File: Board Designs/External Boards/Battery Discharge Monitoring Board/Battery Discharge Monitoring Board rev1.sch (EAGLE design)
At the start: 75 parts

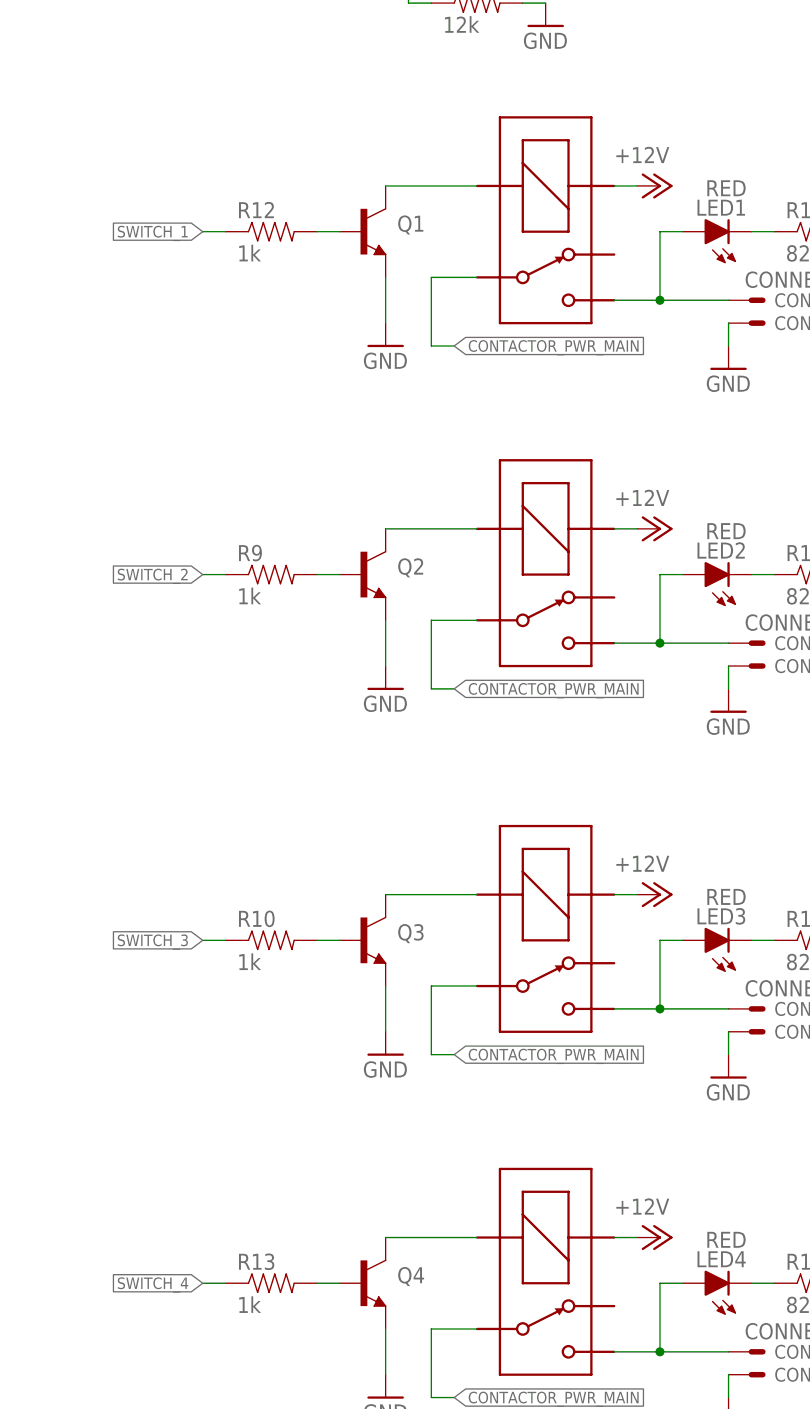
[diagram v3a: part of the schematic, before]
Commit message: Added value for BJTs indicating part number
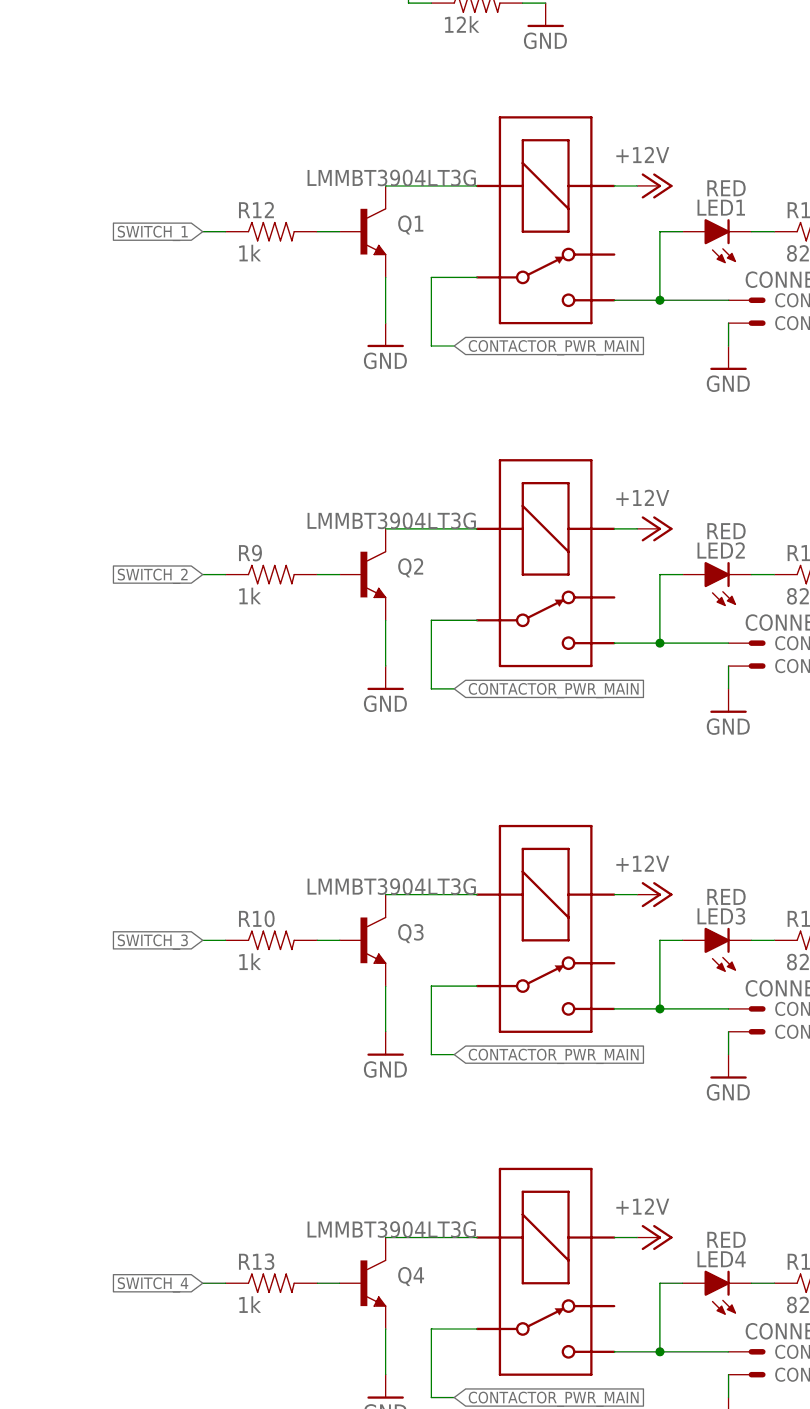
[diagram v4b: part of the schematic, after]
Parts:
- Q1, Q2, Q3, Q4: value (none) -> LMMBT3904LT3G
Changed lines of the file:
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@@
 <part name="P+14" library="supply1" library_urn="urn:adsk.eagle:library:371" deviceset="+5V" device=""/>
 <part name="R11" library="HyTechDevices" deviceset="RESISTOR" device="0805-RES" value="120"/>
-<part name="Q1" library="HyTechDevices" deviceset="BJT_NPN" device="SOT"/>
+<part name="Q1" library="HyTechDevices" deviceset="BJT_NPN" device="SOT" value="LMMBT3904LT3G"/>
 <part name="R12" library="HyTechDevices" deviceset="RESISTOR" device="0805-RES" value="1k"/>
 <part name="GND29" library="supply1" library_urn="urn:adsk.eagle:library:371" deviceset="GND" device=""/>
@@
 <part name="GND30" library="supply1" library_urn="urn:adsk.eagle:library:371" deviceset="GND" device=""/>
 <part name="GND26" library="supply1" library_urn="urn:adsk.eagle:library:371" deviceset="GND" device=""/>
-<part name="Q2" library="HyTechDevices" deviceset="BJT_NPN" device="SOT"/>
+<part name="Q2" library="HyTechDevices" deviceset="BJT_NPN" device="SOT" value="LMMBT3904LT3G"/>
 <part name="R9" library="HyTechDevices" deviceset="RESISTOR" device="0805-RES" value="1k"/>
 <part name="GND31" library="supply1" library_urn="urn:adsk.eagle:library:371" deviceset="GND" device=""/>
@@
 <part name="CONT_2" library="HyTechDevices" deviceset="CONNECTOR-2" device=""/>
 <part name="GND32" library="supply1" library_urn="urn:adsk.eagle:library:371" deviceset="GND" device=""/>
-<part name="Q3" library="HyTechDevices" deviceset="BJT_NPN" device="SOT"/>
+<part name="Q3" library="HyTechDevices" deviceset="BJT_NPN" device="SOT" value="LMMBT3904LT3G"/>
 <part name="R10" library="HyTechDevices" deviceset="RESISTOR" device="0805-RES" value="1k"/>
 <part name="GND33" library="supply1" library_urn="urn:adsk.eagle:library:371" deviceset="GND" device=""/>
@@
 <part name="CONT_3" library="HyTechDevices" deviceset="CONNECTOR-2" device=""/>
 <part name="GND34" library="supply1" library_urn="urn:adsk.eagle:library:371" deviceset="GND" device=""/>
-<part name="Q4" library="HyTechDevices" deviceset="BJT_NPN" device="SOT"/>
+<part name="Q4" library="HyTechDevices" deviceset="BJT_NPN" device="SOT" value="LMMBT3904LT3G"/>
 <part name="R13" library="HyTechDevices" deviceset="RESISTOR" device="0805-RES" value="1k"/>
 <part name="GND35" library="supply1" library_urn="urn:adsk.eagle:library:371" deviceset="GND" device=""/>
@@
 <instance part="Q1" gate="G$1" x="236.22" y="142.24" smashed="yes">
 <attribute name="NAME" x="240.03" y="142.24" size="1.778" layer="95"/>
-<attribute name="VALUE" x="240.03" y="139.7" size="1.778" layer="96"/>
+<attribute name="VALUE" x="229.87" y="147.32" size="1.778" layer="96"/>
 </instance>
 <instance part="R12" gate="G$1" x="226.06" y="142.24" smashed="yes">
@@
 <instance part="Q2" gate="G$1" x="236.22" y="104.14" smashed="yes">
 <attribute name="NAME" x="240.03" y="104.14" size="1.778" layer="95"/>
-<attribute name="VALUE" x="240.03" y="101.6" size="1.778" layer="96"/>
+<attribute name="VALUE" x="229.87" y="109.22" size="1.778" layer="96"/>
 </instance>
 <instance part="R9" gate="G$1" x="226.06" y="104.14" smashed="yes">
@@
 <instance part="Q3" gate="G$1" x="236.22" y="63.5" smashed="yes">
 <attribute name="NAME" x="240.03" y="63.5" size="1.778" layer="95"/>
-<attribute name="VALUE" x="240.03" y="60.96" size="1.778" layer="96"/>
+<attribute name="VALUE" x="229.87" y="68.58" size="1.778" layer="96"/>
 </instance>
 <instance part="R10" gate="G$1" x="226.06" y="63.5" smashed="yes">
@@
 <instance part="Q4" gate="G$1" x="236.22" y="25.4" smashed="yes">
 <attribute name="NAME" x="240.03" y="25.4" size="1.778" layer="95"/>
-<attribute name="VALUE" x="240.03" y="22.86" size="1.778" layer="96"/>
+<attribute name="VALUE" x="229.87" y="30.48" size="1.778" layer="96"/>
 </instance>
 <instance part="R13" gate="G$1" x="226.06" y="25.4" smashed="yes">
